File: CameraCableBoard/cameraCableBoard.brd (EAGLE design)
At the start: 160 x 100 mm, 1 part, among them J2 FLEXCABLE-SFW15R-1STE1LF

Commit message: Worked on camera board
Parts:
- added U$1: DB15, SparkFun-Retired:DB15
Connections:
- new net 3.3V: J2.15
- new net CON_CLKN: J2.8
- new net CON_CLKP: J2.9
- new net CON_D0N: J2.2, U$1.6
- new net CON_D0P: J2.3, U$1.11
- new net CON_D1N: J2.5
- new net CON_D1P: J2.6
- new net ENABLE: J2.11
- new net GND: J2.1, J2.10, J2.4, J2.7, U$1.1, U$1.7
- new net N$10: U$1.13
- new net N$11: U$1.8
- new net N$12: U$1.9
- new net N$13: U$1.14
- new net N$14: U$1.10
- new net N$15: U$1.15
- new net N$2: U$1.2
- new net N$3: U$1.3
- new net N$4: U$1.4
- new net N$5: U$1.5
- new net N$9: U$1.12
- new net SCL: J2.13
- new net SDA: J2.14
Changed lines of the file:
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@@
 <attribute name="VALUE" x="-30.8408" y="6.20466875" size="1.272509375" layer="27"/>
+</element>
+<element name="U$1" library="SparkFun-Retired" library_urn="urn:adsk.eagle:library:533" package="DB15" value="DB15" x="-15.24" y="-12.7" smashed="yes">
+<attribute name="NAME" x="-16.51" y="-10.922" size="0.6096" layer="25" font="vector" ratio="20"/>
+<attribute name="VALUE" x="-16.51" y="-11.938" size="0.6096" layer="27" font="vector" ratio="20"/>
 </element>
 </elements>
 <signals>
+<signal name="GND">
+<contactref element="J2" pad="1"/>
+<contactref element="J2" pad="4"/>
+<contactref element="J2" pad="7"/>
+<contactref element="J2" pad="10"/>
+<contactref element="U$1" pad="1"/>
+<contactref element="U$1" pad="7"/>
+<wire x1="-18.41" y1="-17.78" x2="-19.56" y2="-20.32" width="0" layer="19" extent="1-1"/>
+<wire x1="-18.32" y1="13.97" x2="-18.41" y2="-17.78" width="0" layer="19" extent="1-1"/>
+<wire x1="-21.32" y1="13.97" x2="-18.32" y2="13.97" width="0" layer="19" extent="1-1"/>
+<wire x1="-24.32" y1="13.97" x2="-21.32" y2="13.97" width="0" layer="19" extent="1-1"/>
+<wire x1="-27.32" y1="13.97" x2="-24.32" y2="13.97" width="0" layer="19" extent="1-1"/>
+</signal>
+<signal name="CON_D0N">
+<contactref element="J2" pad="2"/>
+<contactref element="U$1" pad="6"/>
+<wire x1="-26.32" y1="13.97" x2="-20.7" y2="-17.78" width="0" layer="19" extent="1-1"/>
+</signal>
+<signal name="CON_D0P">
+<contactref element="J2" pad="3"/>
+<contactref element="U$1" pad="11"/>
+<wire x1="-25.32" y1="13.97" x2="-19.56" y2="-15.24" width="0" layer="19" extent="1-1"/>
+</signal>
+<signal name="CON_D1N">
+<contactref element="J2" pad="5"/>
+</signal>
+<signal name="CON_D1P">
+<contactref element="J2" pad="6"/>
+</signal>
+<signal name="CON_CLKN">
+<contactref element="J2" pad="8"/>
+</signal>
+<signal name="CON_CLKP">
+<contactref element="J2" pad="9"/>
+</signal>
+<signal name="ENABLE">
+<contactref element="J2" pad="11"/>
+</signal>
+<signal name="SCL">
+<contactref element="J2" pad="13"/>
+</signal>
+<signal name="SDA">
+<contactref element="J2" pad="14"/>
+</signal>
+<signal name="3.3V">
+<contactref element="J2" pad="15"/>
+</signal>
+<signal name="N$2">
+<contactref element="U$1" pad="2"/>
+</signal>
+<signal name="N$3">
+<contactref element="U$1" pad="3"/>
+</signal>
+<signal name="N$4">
+<contactref element="U$1" pad="4"/>
+</signal>
+<signal name="N$5">
+<contactref element="U$1" pad="5"/>
+</signal>
+<signal name="N$9">
+<contactref element="U$1" pad="12"/>
+</signal>
+<signal name="N$10">
+<contactref element="U$1" pad="13"/>
+</signal>
+<signal name="N$11">
+<contactref element="U$1" pad="8"/>
+</signal>
+<signal name="N$12">
+<contactref element="U$1" pad="9"/>
+</signal>
+<signal name="N$13">
+<contactref element="U$1" pad="14"/>
+</signal>
+<signal name="N$14">
+<contactref element="U$1" pad="10"/>
+</signal>
+<signal name="N$15">
+<contactref element="U$1" pad="15"/>
+</signal>
 </signals>
 <mfgpreviewcolors>
@@
 </board>
 </drawing>
+<compatibility>
+<note version="8.2" severity="warning">
+Since Version 8.2, EAGLE supports online libraries. The ids
+of those online libraries will not be understood (or retained)
+with this version.
+</note>
+</compatibility>
 </eagle>

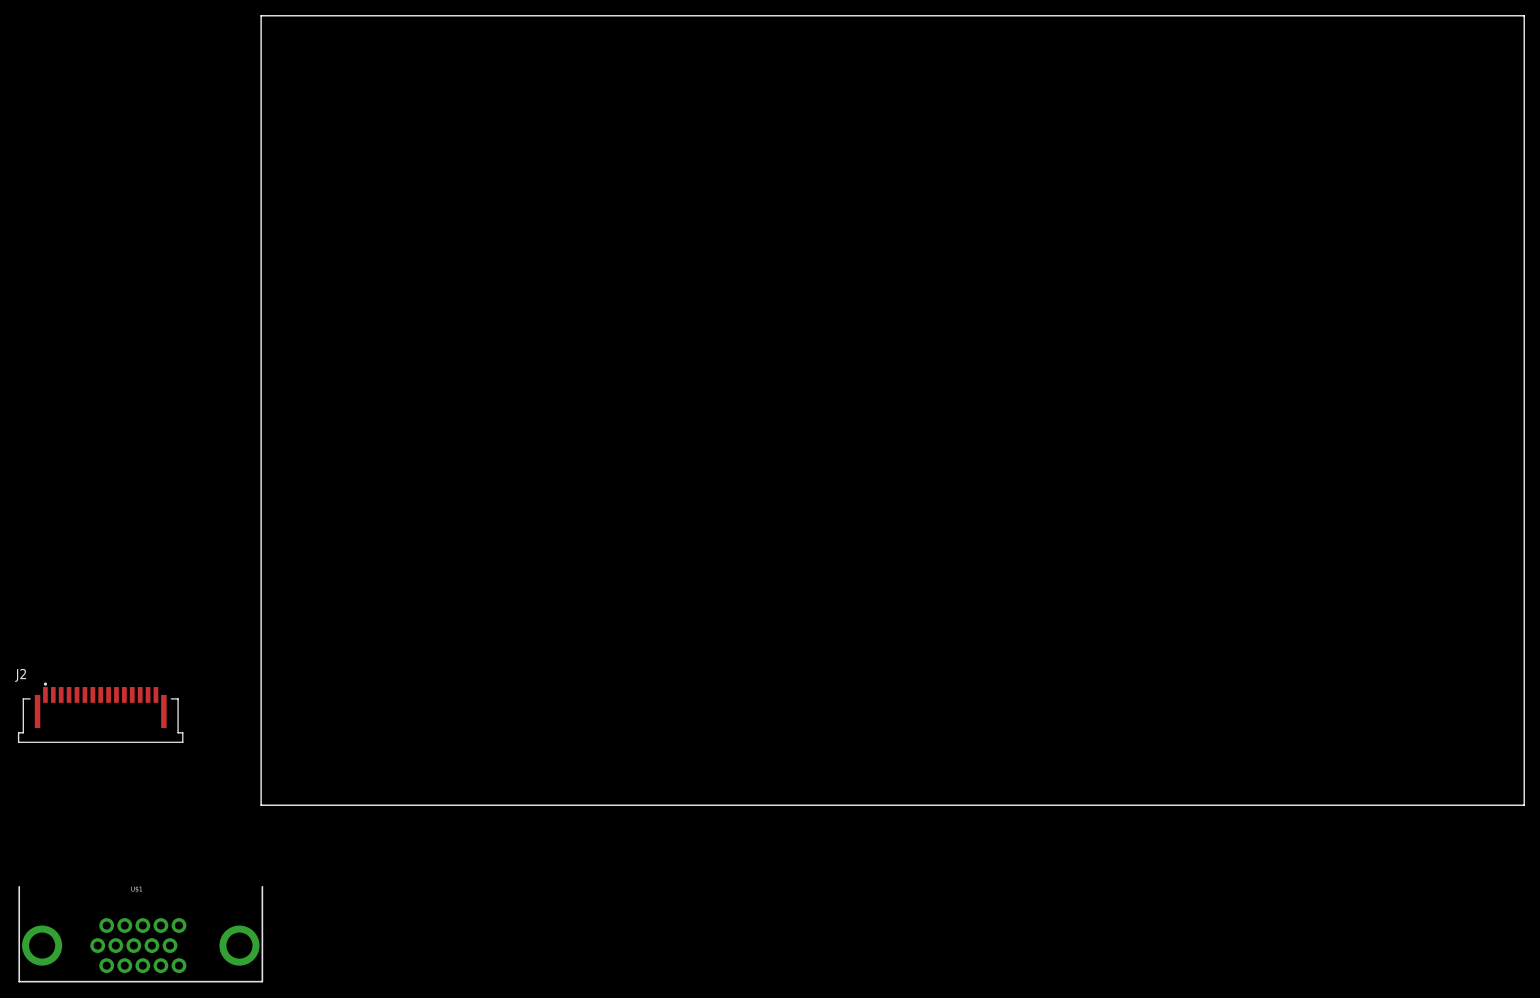
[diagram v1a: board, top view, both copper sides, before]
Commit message: Added board-edge db15, ready to route camera signal converter board
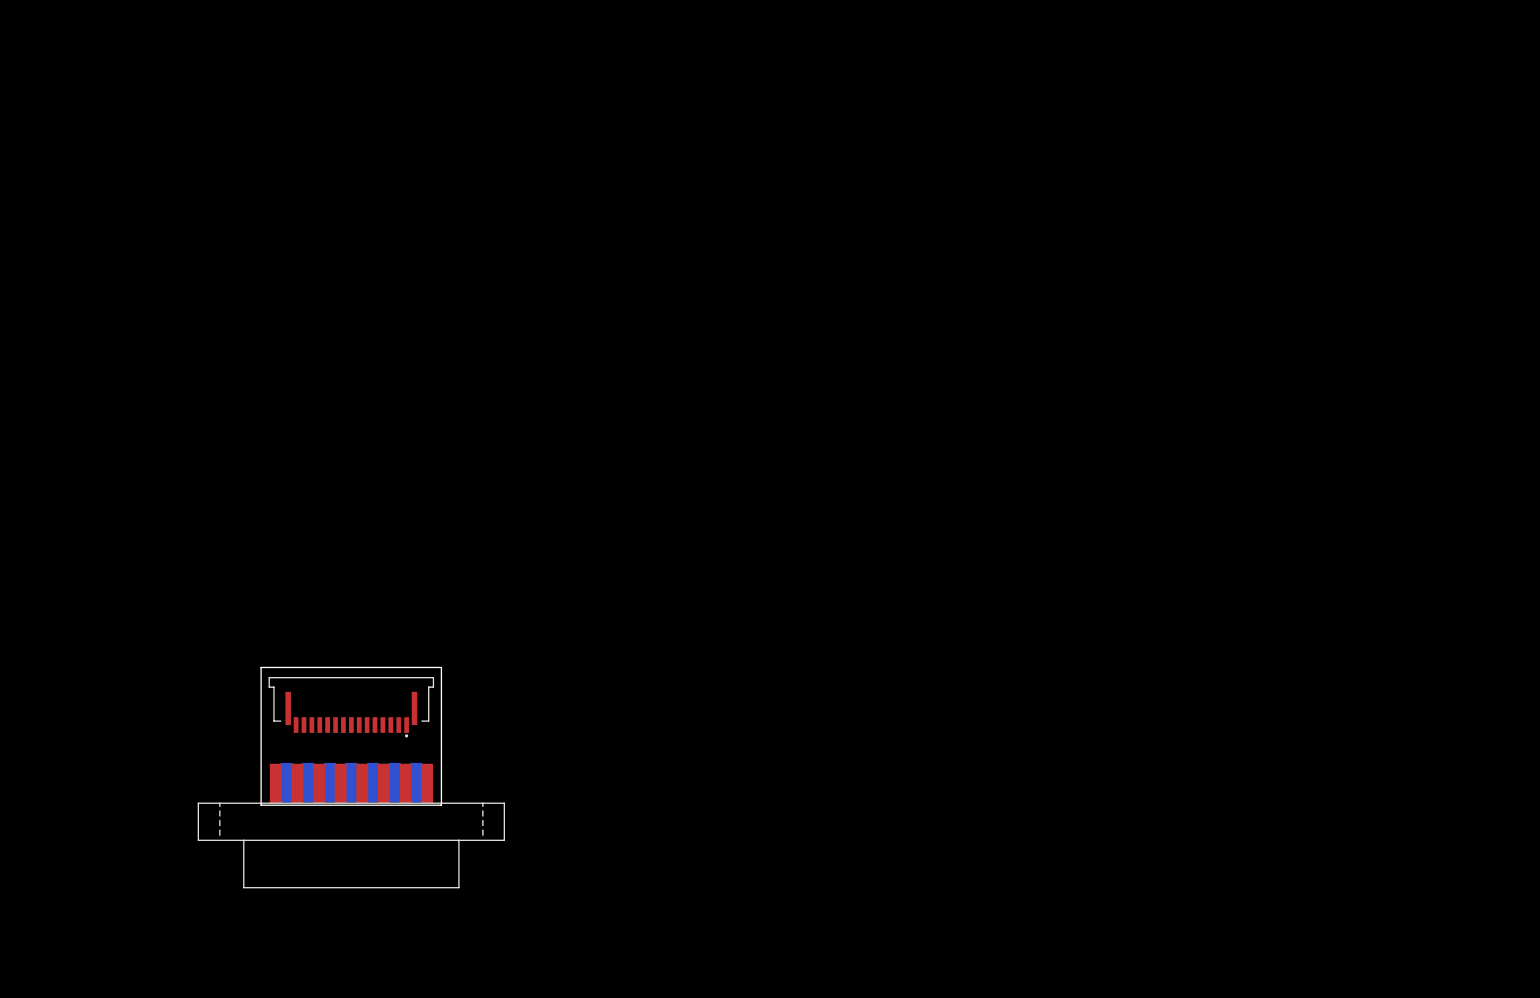
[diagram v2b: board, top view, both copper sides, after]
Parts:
- removed U$1: DB15, SparkFun-Retired:DB15
- added U$2: DB15-BOARD-EDGE, RPi-Parts:DB15-BOARD-EDGE
- moved J2 32.0 mm to (11.4, 10.2), turned to 180 degrees
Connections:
- removed net 3.3V: J2.15
- removed net CON_CLKN: J2.8
- removed net CON_CLKP: J2.9
- removed net CON_D0N: J2.2, U$1.6
- removed net CON_D0P: J2.3, U$1.11
- removed net CON_D1N: J2.5
- removed net CON_D1P: J2.6
- removed net ENABLE: J2.11
- removed net GND: J2.1, J2.10, J2.4, J2.7, U$1.1, U$1.7
- removed net N$10: U$1.13
- removed net N$11: U$1.8
- removed net N$12: U$1.9
- removed net N$13: U$1.14
- removed net N$14: U$1.10
- removed net N$15: U$1.15
- removed net N$2: U$1.2
- removed net N$3: U$1.3
- removed net N$4: U$1.4
- removed net N$5: U$1.5
- removed net N$9: U$1.12
- removed net SCL: J2.13
- removed net SDA: J2.14
- new net CAM1: J2.1, U$2.P8
- new net CAM10: J2.10, U$2.P11
- new net CAM11: J2.11, U$2.P3
- new net CAM12: J2.12, U$2.P10
- new net CAM13: J2.13, U$2.P2
- new net CAM14: J2.14, U$2.P9
- new net CAM15: J2.15, U$2.P1
- new net CAM2: J2.2, U$2.P15
- new net CAM3: J2.3, U$2.P7
- new net CAM4: J2.4, U$2.P14
- new net CAM5: J2.5, U$2.P6
- new net CAM6: J2.6, U$2.P13
- new net CAM7: J2.7, U$2.P5
- new net CAM8: J2.8, U$2.P12
- new net CAM9: J2.9, U$2.P4
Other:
- board size 160 x 100 mm -> 22.8 x 17.4 mm

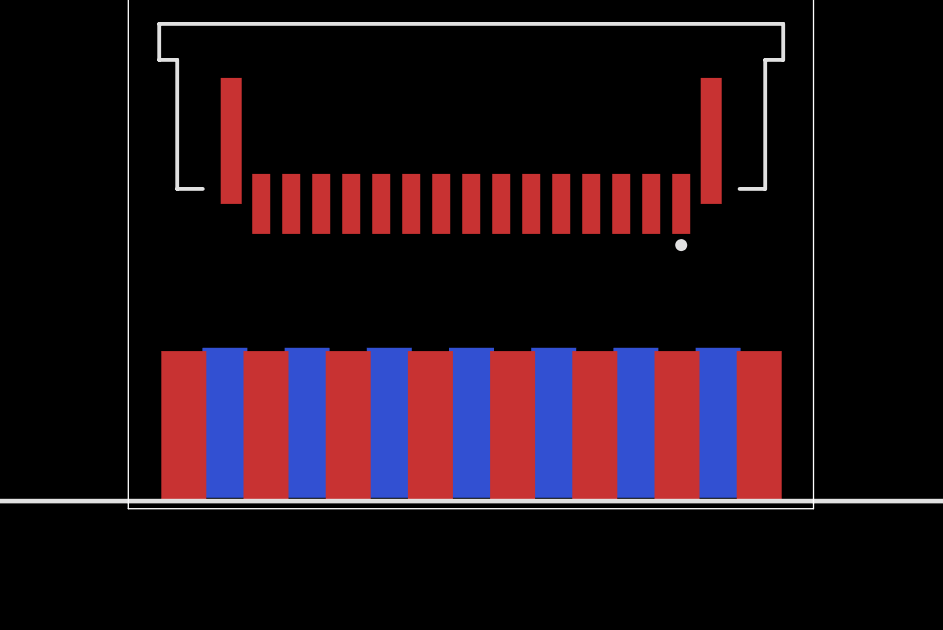
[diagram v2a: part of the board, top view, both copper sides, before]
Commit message: Routed camera converter board|
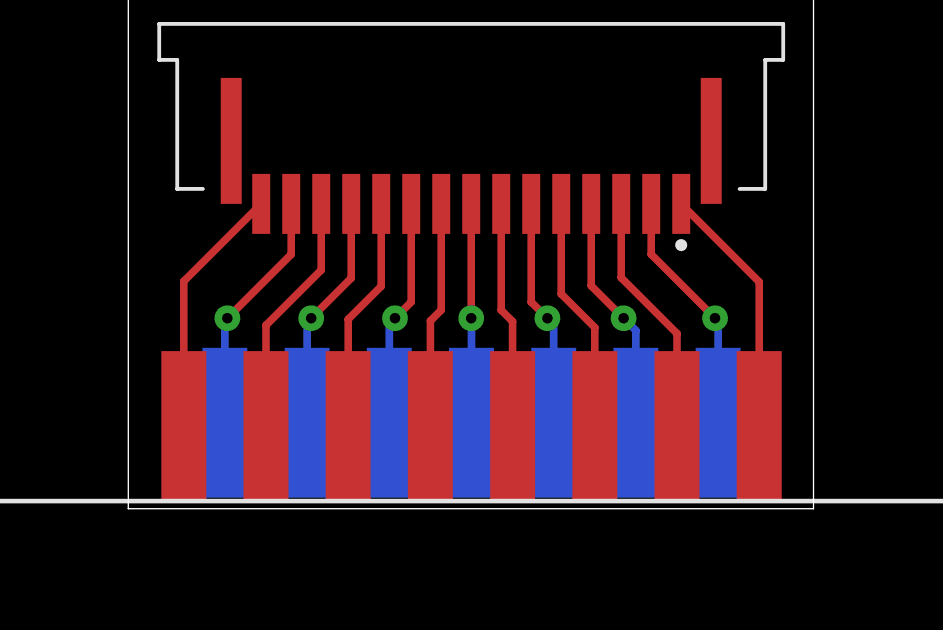
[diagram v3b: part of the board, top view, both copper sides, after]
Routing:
- net CAM1: track 0.00 -> 8.48 mm
- net CAM15: track 0.00 -> 8.47 mm
- net CAM2: track 0.00 -> 8.22 mm, vias 0 -> 1
- net CAM14: track 0.00 -> 8.21 mm, vias 0 -> 1
- net CAM3: track 0.00 -> 8.18 mm
- net CAM13: track 0.00 -> 8.17 mm
- net CAM4: track 0.00 -> 7.91 mm, vias 0 -> 1
- net CAM12: track 0.00 -> 7.90 mm, vias 0 -> 1
- net CAM5: track 0.00 -> 7.87 mm
- net CAM11: track 0.00 -> 7.86 mm
- net CAM6: track 0.00 -> 7.61 mm, vias 0 -> 1
- net CAM10: track 0.00 -> 7.60 mm, vias 0 -> 1
- net CAM7: track 0.00 -> 7.56 mm
- net CAM9: track 0.00 -> 7.56 mm
- net CAM8: track 0.00 -> 7.30 mm, vias 0 -> 1
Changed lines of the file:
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@@
 <setting verticaltext="up"/>
 </settings>
-<grid distance="50" unitdist="mil" unit="mil" style="lines" multiple="1" display="no" altdistance="5" altunitdist="mil" altunit="mil"/>
+<grid distance="25" unitdist="mil" unit="mil" style="lines" multiple="4" display="yes" altdistance="5" altunitdist="mil" altunit="mil"/>
 <layers>
 <layer number="1" name="Top" color="4" fill="1" visible="yes" active="yes"/>
@@
 <contactref element="J2" pad="1"/>
 <contactref element="U$2" pad="P8"/>
-<wire x1="21.03" y1="2.754" x2="18.43" y2="10.16" width="0" layer="19" extent="1-1"/>
+<wire x1="21.03" y1="2.754" x2="21.03" y2="7.56" width="0.254" layer="1"/>
+<wire x1="21.03" y1="7.56" x2="18.43" y2="10.16" width="0.254" layer="1"/>
 </signal>
 <signal name="CAM2">
 <contactref element="J2" pad="2"/>
 <contactref element="U$2" pad="P15"/>
-<wire x1="19.66" y1="2.864" x2="17.43" y2="10.16" width="0" layer="19" extent="1-16"/>
+<wire x1="19.66" y1="2.864" x2="19.66" y2="6.248" width="0.254" layer="16"/>
+<wire x1="19.66" y1="6.248" x2="19.558" y2="6.35" width="0.254" layer="16"/>
+<via x="19.558" y="6.35" extent="1-16" drill="0.35"/>
+<wire x1="19.558" y1="6.35" x2="17.43" y2="8.478" width="0.254" layer="1"/>
+<wire x1="17.43" y1="8.478" x2="17.43" y2="10.16" width="0.254" layer="1"/>
 </signal>
 <signal name="CAM3">
 <contactref element="J2" pad="3"/>
 <contactref element="U$2" pad="P7"/>
-<wire x1="18.29" y1="2.754" x2="16.43" y2="10.16" width="0" layer="19" extent="1-1"/>
+<wire x1="18.29" y1="2.754" x2="18.29" y2="5.84" width="0.254" layer="1"/>
+<wire x1="16.43" y1="7.7" x2="16.43" y2="10.16" width="0.254" layer="1"/>
+<wire x1="18.29" y1="5.84" x2="16.43" y2="7.7" width="0.254" layer="1"/>
 </signal>
 <signal name="CAM4">
 <contactref element="J2" pad="4"/>
 <contactref element="U$2" pad="P14"/>
-<wire x1="16.92" y1="2.864" x2="15.43" y2="10.16" width="0" layer="19" extent="1-16"/>
+<wire x1="16.92" y1="2.864" x2="16.92" y2="5.94" width="0.254" layer="16"/>
+<wire x1="16.92" y1="5.94" x2="16.51" y2="6.35" width="0.254" layer="16"/>
+<via x="16.51" y="6.35" extent="1-16" drill="0.35"/>
+<wire x1="16.51" y1="6.35" x2="15.43" y2="7.43" width="0.254" layer="1"/>
+<wire x1="15.43" y1="7.43" x2="15.43" y2="10.16" width="0.254" layer="1"/>
 </signal>
 <signal name="CAM5">
 <contactref element="J2" pad="5"/>
 <contactref element="U$2" pad="P6"/>
-<wire x1="15.55" y1="2.754" x2="14.43" y2="10.16" width="0" layer="19" extent="1-1"/>
+<wire x1="15.55" y1="2.754" x2="15.55" y2="6.04" width="0.254" layer="1"/>
+<wire x1="14.43" y1="7.16" x2="14.43" y2="10.16" width="0.254" layer="1"/>
+<wire x1="15.55" y1="6.04" x2="14.43" y2="7.16" width="0.254" layer="1"/>
 </signal>
 <signal name="CAM6">
 <contactref element="J2" pad="6"/>
 <contactref element="U$2" pad="P13"/>
-<wire x1="14.18" y1="2.864" x2="13.43" y2="10.16" width="0" layer="19" extent="1-16"/>
+<wire x1="14.18" y1="2.864" x2="14.18" y2="6.14" width="0.254" layer="16"/>
+<wire x1="14.18" y1="6.14" x2="13.97" y2="6.35" width="0.254" layer="16"/>
+<via x="13.97" y="6.35" extent="1-16" drill="0.35"/>
+<wire x1="13.97" y1="6.35" x2="13.43" y2="6.89" width="0.254" layer="1"/>
+<wire x1="13.43" y1="6.89" x2="13.43" y2="10.16" width="0.254" layer="1"/>
 </signal>
 <signal name="CAM7">
 <contactref element="J2" pad="7"/>
 <contactref element="U$2" pad="P5"/>
-<wire x1="12.81" y1="2.754" x2="12.43" y2="10.16" width="0" layer="19" extent="1-1"/>
+<wire x1="12.81" y1="2.754" x2="12.81" y2="6.24" width="0.254" layer="1"/>
+<wire x1="12.43" y1="6.62" x2="12.43" y2="10.16" width="0.254" layer="1"/>
+<wire x1="12.81" y1="6.24" x2="12.43" y2="6.62" width="0.254" layer="1"/>
 </signal>
 <signal name="CAM8">
 <contactref element="J2" pad="8"/>
 <contactref element="U$2" pad="P12"/>
-<wire x1="11.44" y1="2.864" x2="11.43" y2="10.16" width="0" layer="19" extent="1-16"/>
+<wire x1="11.44" y1="2.864" x2="11.44" y2="6.34" width="0.254" layer="16"/>
+<wire x1="11.44" y1="6.34" x2="11.43" y2="6.35" width="0.254" layer="16"/>
+<via x="11.43" y="6.35" extent="1-16" drill="0.35"/>
+<wire x1="11.43" y1="6.35" x2="11.43" y2="10.16" width="0.254" layer="1"/>
 </signal>
 <signal name="CAM9">
 <contactref element="J2" pad="9"/>
 <contactref element="U$2" pad="P4"/>
-<wire x1="10.07" y1="2.754" x2="10.43" y2="10.16" width="0" layer="19" extent="1-1"/>
+<wire x1="10.07" y1="2.754" x2="10.07" y2="6.26" width="0.254" layer="1"/>
+<wire x1="10.43" y1="6.62" x2="10.43" y2="10.16" width="0.254" layer="1"/>
+<wire x1="10.07" y1="6.26" x2="10.43" y2="6.62" width="0.254" layer="1"/>
 </signal>
 <signal name="CAM10">
 <contactref element="J2" pad="10"/>
 <contactref element="U$2" pad="P11"/>
-<wire x1="8.7" y1="2.864" x2="9.43" y2="10.16" width="0" layer="19" extent="1-16"/>
+<wire x1="8.7" y1="2.864" x2="8.7" y2="6.16" width="0.254" layer="16"/>
+<wire x1="8.7" y1="6.16" x2="8.89" y2="6.35" width="0.254" layer="16"/>
+<via x="8.89" y="6.35" extent="1-16" drill="0.35"/>
+<wire x1="8.89" y1="6.35" x2="9.43" y2="6.89" width="0.254" layer="1"/>
+<wire x1="9.43" y1="6.89" x2="9.43" y2="10.16" width="0.254" layer="1"/>
 </signal>
 <signal name="CAM11">
 <contactref element="J2" pad="11"/>
 <contactref element="U$2" pad="P3"/>
-<wire x1="7.33" y1="2.754" x2="8.43" y2="10.16" width="0" layer="19" extent="1-1"/>
+<wire x1="7.33" y1="2.754" x2="7.33" y2="6.314" width="0.254" layer="1"/>
+<wire x1="8.43" y1="7.414" x2="8.43" y2="10.16" width="0.254" layer="1"/>
+<wire x1="7.33" y1="6.314" x2="8.43" y2="7.414" width="0.254" layer="1"/>
 </signal>
 <signal name="CAM12">
 <contactref element="J2" pad="12"/>
 <contactref element="U$2" pad="P10"/>
-<wire x1="5.96" y1="2.864" x2="7.43" y2="10.16" width="0" layer="19" extent="1-16"/>
+<wire x1="5.96" y1="2.864" x2="5.96" y2="6.214" width="0.254" layer="16"/>
+<wire x1="5.96" y1="6.214" x2="6.096" y2="6.35" width="0.254" layer="16"/>
+<via x="6.096" y="6.35" extent="1-16" drill="0.35"/>
+<wire x1="6.096" y1="6.35" x2="7.43" y2="7.684" width="0.254" layer="1"/>
+<wire x1="7.43" y1="7.684" x2="7.43" y2="10.16" width="0.254" layer="1"/>
 </signal>
 <signal name="CAM13">
 <contactref element="J2" pad="13"/>
 <contactref element="U$2" pad="P2"/>
-<wire x1="4.59" y1="2.754" x2="6.43" y2="10.16" width="0" layer="19" extent="1-1"/>
+<wire x1="4.59" y1="2.754" x2="4.59" y2="6.114" width="0.254" layer="1"/>
+<wire x1="6.43" y1="7.954" x2="6.43" y2="10.16" width="0.254" layer="1"/>
+<wire x1="4.59" y1="6.114" x2="6.43" y2="7.954" width="0.254" layer="1"/>
 </signal>
 <signal name="CAM14">
 <contactref element="J2" pad="14"/>
 <contactref element="U$2" pad="P9"/>
-<wire x1="3.22" y1="2.864" x2="5.43" y2="10.16" width="0" layer="19" extent="1-16"/>
+<wire x1="3.22" y1="2.864" x2="3.22" y2="6.268" width="0.254" layer="16"/>
+<wire x1="3.22" y1="6.268" x2="3.302" y2="6.35" width="0.254" layer="16"/>
+<via x="3.302" y="6.35" extent="1-16" drill="0.35"/>
+<wire x1="5.43" y1="10.16" x2="5.43" y2="8.478" width="0.254" layer="1"/>
+<wire x1="5.43" y1="8.478" x2="3.302" y2="6.35" width="0.254" layer="1"/>
 </signal>
 <signal name="CAM15">
 <contactref element="J2" pad="15"/>
 <contactref element="U$2" pad="P1"/>
-<wire x1="1.85" y1="2.754" x2="4.43" y2="10.16" width="0" layer="19" extent="1-1"/>
+<wire x1="1.85" y1="2.754" x2="1.85" y2="7.58" width="0.254" layer="1"/>
+<wire x1="1.85" y1="7.58" x2="4.43" y2="10.16" width="0.254" layer="1"/>
 </signal>
 </signals>
